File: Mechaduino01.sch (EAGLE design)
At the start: 70 parts, among them IC1 SAMD21G18A-AUT, IC2 AP2202-ADJ, Q1 2.5A/30V, Q2 NFET, Q3 BSS138, Q4 BSS138, Q5 BSS138, U3 74AHC1G125, Y1 32,768Khz

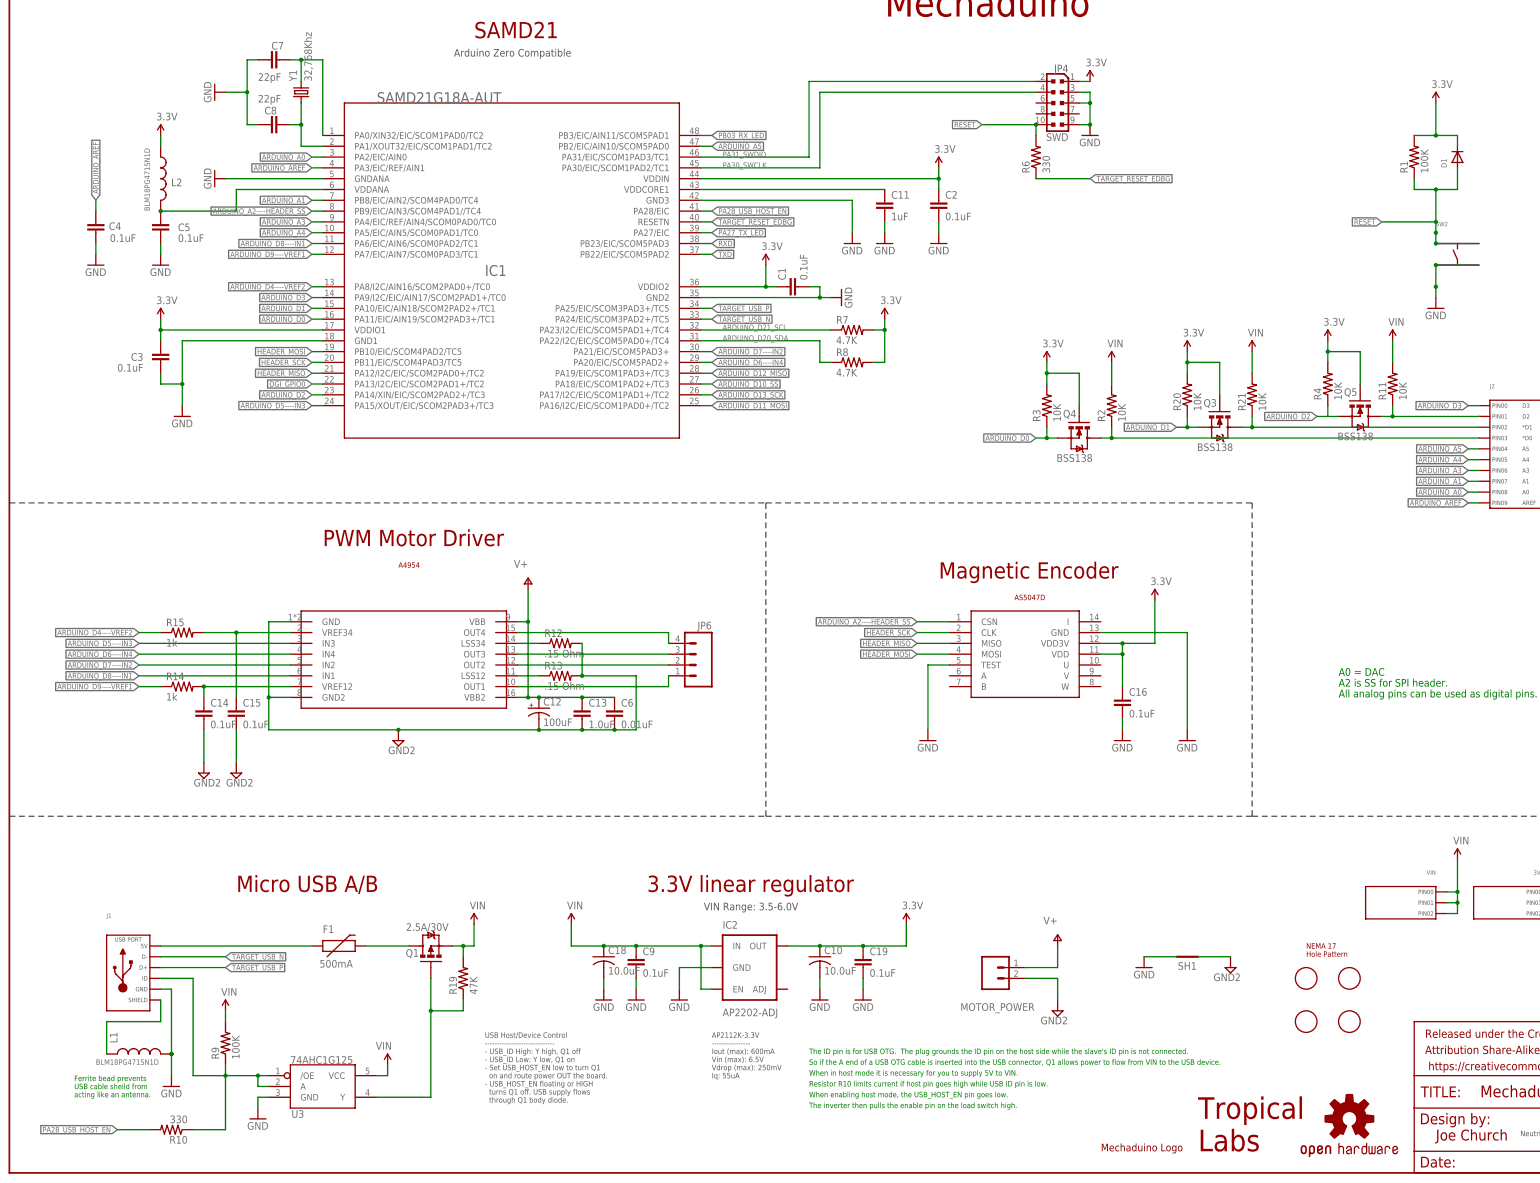
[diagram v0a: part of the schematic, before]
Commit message: moved IO headers down 0.01
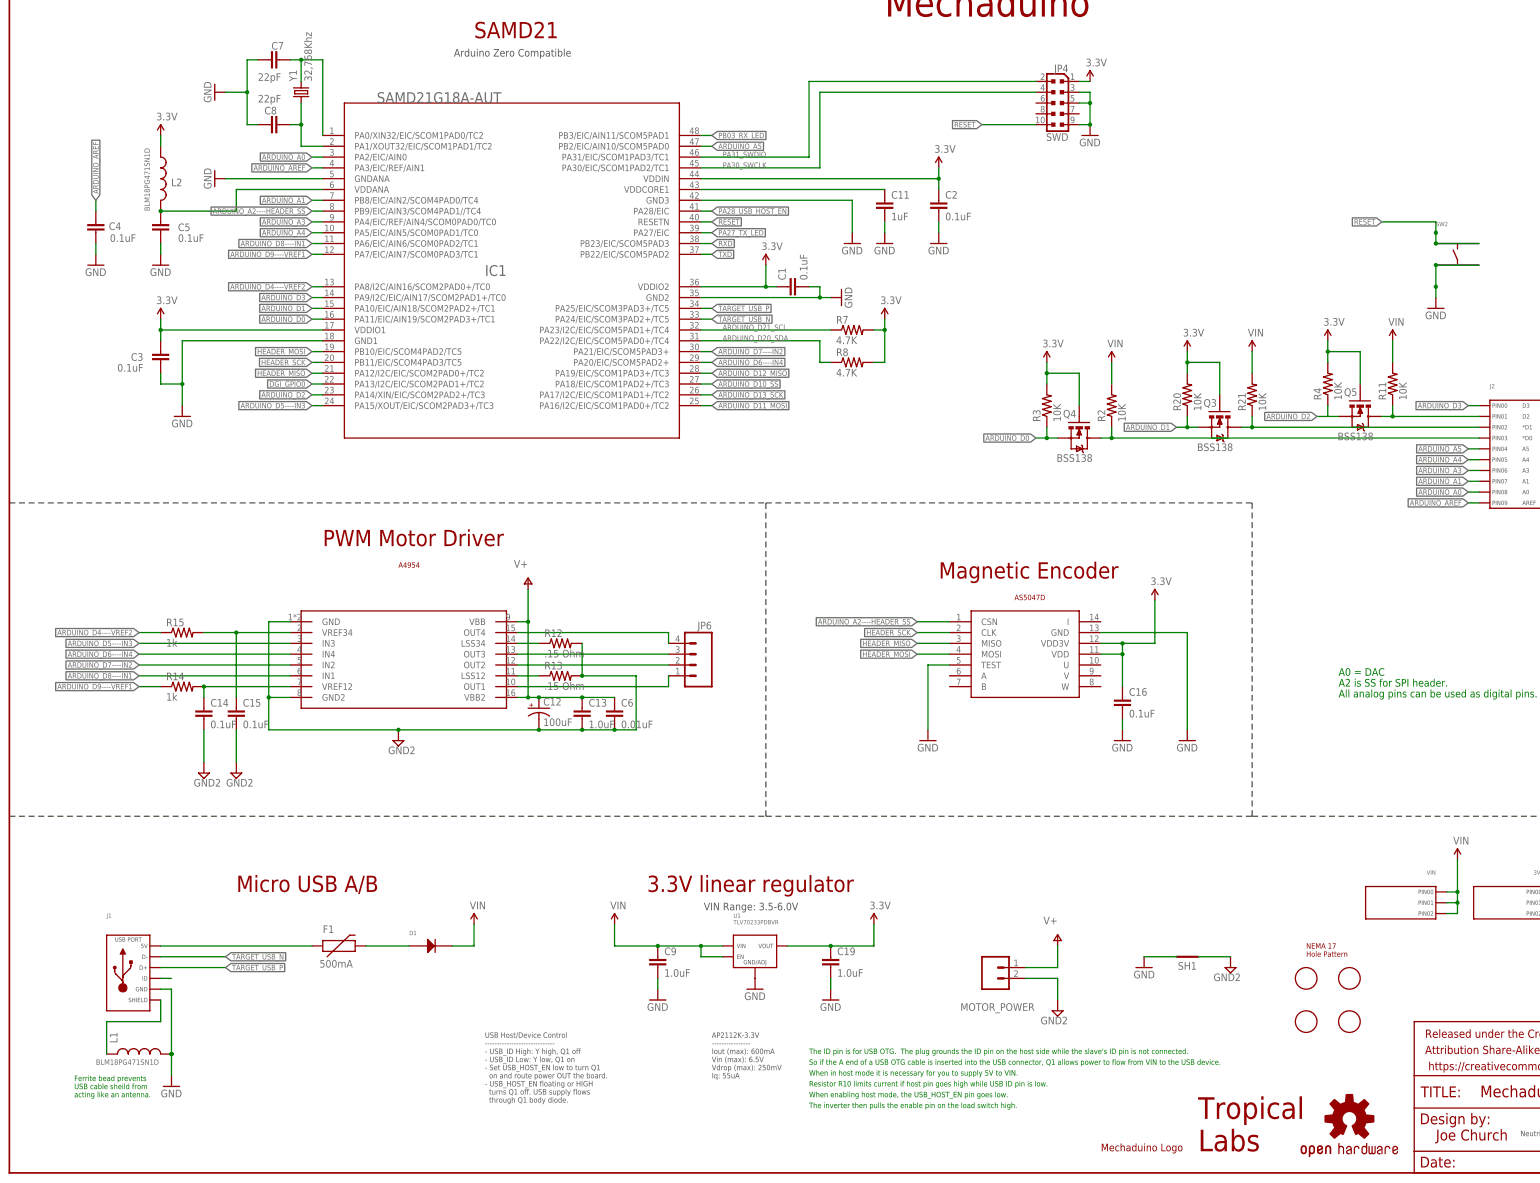
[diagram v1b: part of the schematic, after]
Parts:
- removed C10, C18: 10.0uF, rcl:C-USC0805
- removed IC2: AP2202-ADJ, SparkFun-PowerIC:AP2202-ADJ
- removed Q1: 2.5A/30V, SparkFun-DiscreteSemi:MOSFET-PCHANNELDMG2307L
- removed R1, R9: 100K, adafruit:R-US_R0402-VISHAY
- removed R10, R6: 330, adafruit:R-US_R0402-VISHAY
- removed R19: 47K, SparkFun-Resistors:47KOHM1/10W1%(0603)
- removed U3: 74AHC1G125, SparkFun-DigitalIC:74AHC1G125
- added U1: TLV70233PDBVR, MF_IC_Power:TLV70233PDBVR
- C19, C9: value 0.1uF -> 1.0uF
- D1: device adafruit:DIODESOD-523 -> MF_Discrete_Semiconductor:DIODE_SMA
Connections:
- removed net N$34: Q1.G, R19.1, U3.Y
- removed net TARGET_RESET_EDBG: IC1.RESETN, R6.1
- net 3.3V: now also U1.VOUT; no longer C10.1, D1.C, IC2.OUT, R1.2
- net GND: now also U1.GND/ADJ; no longer C10.2, C18.2, IC2.GND, U3.GND
- net N$33: now also D1.ANODE; no longer Q1.D
- net N$7: no longer R10.1, R9.1, U3./OE, U3.A
- net PA28_USB_HOST_EN: no longer R10.2
- net RESET: now also IC1.RESETN; no longer D1.A, R1.1, R6.2
- net VIN: now also D1.CATHODE, U1.EN, U1.VIN; no longer C18.1, IC2.EN, IC2.IN, Q1.S, R19.2, R9.2, U3.VCC
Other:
- moved on the sheet: C19, C9, D1

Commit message: moved things around
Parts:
- D1: device MF_Discrete_Semiconductor:DIODE_SMA -> MF_Discrete_Semiconductor:DIODE_SOD-123
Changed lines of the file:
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@@
 <part name="R11" library="adafruit" deviceset="R-US_" device="R0402-VISHAY" value="10K"/>
 <part name="U1" library="MF_IC_Power" deviceset="TLV702" device="33PDBVR"/>
-<part name="D1" library="MF_Discrete_Semiconductor" deviceset="DIODE" device="_SMA"/>
+<part name="D1" library="MF_Discrete_Semiconductor" deviceset="DIODE" device="_SOD-123"/>
 </parts>
 <sheets>

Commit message: commit after rollback issues
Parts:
- added Q1: BSS138, SparkFun:MOSFET-NCHANNELSMD
- added R1, R6: 10K, adafruit:R-US_R0402-VISHAY
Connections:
- new net HV4: J2.PIN0, Q1.D, R6.1
- net 3.3V: now also Q1.G, R1.2
- net ARDUINO_D3: now also Q1.S, R1.1; no longer J2.PIN0
- net VIN: now also R6.2
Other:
- moved on the sheet: Q3, Q4, Q5, R11, R2, R20, R21, R3, R4

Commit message: updated caps
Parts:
- C7, C8: value 22pF -> 18pF
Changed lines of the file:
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@@
 <part name="C5" library="swift" deviceset="CAP" device="0402" value="0.1uF"/>
 <part name="GND41" library="PowerTags" deviceset="GND" device=""/>
-<part name="C7" library="swift" deviceset="CAP" device="0402" value="22pF"/>
-<part name="C8" library="swift" deviceset="CAP" device="0402" value="22pF"/>
+<part name="C7" library="swift" deviceset="CAP" device="0402" value="18pF"/>
+<part name="C8" library="swift" deviceset="CAP" device="0402" value="18pF"/>
 <part name="LED1" library="Opto" deviceset="0044_KPT-2012YC" device="" value="Green"/>
 <part name="R7" library="adafruit" deviceset="R-US_" device="R0402-VISHAY" value="4.7K"/>

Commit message: reday to order
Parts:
- LOGO4: value OSHW-LOGOL-COPPER -> OSHW-LOGOMOD; device SparkFun-Aesthetics:OSHW-LOGOL-COPPER -> SparkFun-Aesthetics:OSHW-LOGOMOD
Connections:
- new net A: U$4.A
- new net B: U$4.B
- new net I: U$4.I
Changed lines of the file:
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@@
 <grid distance="0.1" unitdist="inch" unit="inch" style="lines" multiple="1" display="no" altdistance="0.01" altunitdist="inch" altunit="inch"/>
 <layers>
-<layer number="1" name="Top" color="4" fill="1" visible="no" active="no"/>
-<layer number="16" name="Bottom" color="1" fill="1" visible="no" active="no"/>
-<layer number="17" name="Pads" color="2" fill="1" visible="no" active="no"/>
-<layer number="18" name="Vias" color="2" fill="1" visible="no" active="no"/>
-<layer number="19" name="Unrouted" color="15" fill="1" visible="no" active="no"/>
-<layer number="20" name="Dimension" color="15" fill="1" visible="no" active="no"/>
-<layer number="21" name="tPlace" color="7" fill="1" visible="no" active="no"/>
-<layer number="22" name="bPlace" color="15" fill="1" visible="no" active="no"/>
-<layer number="23" name="tOrigins" color="15" fill="1" visible="no" active="no"/>
-<layer number="24" name="bOrigins" color="15" fill="1" visible="no" active="no"/>
-<layer number="25" name="tNames" color="10" fill="1" visible="no" active="no"/>
-<layer number="26" name="bNames" color="7" fill="1" visible="no" active="no"/>
-<layer number="27" name="tValues" color="7" fill="1" visible="no" active="no"/>
-<layer number="28" name="bValues" color="7" fill="1" visible="no" active="no"/>
+<layer number="1" name="Top" color="4" fill="1" visible="yes" active="no"/>
+<layer number="16" name="Bottom" color="1" fill="1" visible="yes" active="no"/>
+<layer number="17" name="Pads" color="2" fill="1" visible="yes" active="no"/>
+<layer number="18" name="Vias" color="2" fill="1" visible="yes" active="no"/>
+<layer number="19" name="Unrouted" color="15" fill="1" visible="yes" active="no"/>
+<layer number="20" name="Dimension" color="15" fill="1" visible="yes" active="no"/>
+<layer number="21" name="tPlace" color="7" fill="1" visible="yes" active="no"/>
+<layer number="22" name="bPlace" color="15" fill="1" visible="yes" active="no"/>
+<layer number="23" name="tOrigins" color="15" fill="1" visible="yes" active="no"/>
+<layer number="24" name="bOrigins" color="15" fill="1" visible="yes" active="no"/>
+<layer number="25" name="tNames" color="10" fill="1" visible="yes" active="no"/>
+<layer number="26" name="bNames" color="7" fill="1" visible="yes" active="no"/>
+<layer number="27" name="tValues" color="7" fill="1" visible="yes" active="no"/>
+<layer number="28" name="bValues" color="7" fill="1" visible="yes" active="no"/>
 <layer number="29" name="tStop" color="7" fill="3" visible="no" active="no"/>
 <layer number="30" name="bStop" color="7" fill="6" visible="no" active="no"/>
@@
 <layer number="35" name="tGlue" color="7" fill="4" visible="no" active="no"/>
 <layer number="36" name="bGlue" color="7" fill="5" visible="no" active="no"/>
-<layer number="37" name="tTest" color="7" fill="1" visible="no" active="no"/>
-<layer number="38" name="bTest" color="7" fill="1" visible="no" active="no"/>
+<layer number="37" name="tTest" color="7" fill="1" visible="yes" active="no"/>
+<layer number="38" name="bTest" color="7" fill="1" visible="yes" active="no"/>
 <layer number="39" name="tKeepout" color="4" fill="11" visible="no" active="no"/>
 <layer number="40" name="bKeepout" color="1" fill="11" visible="no" active="no"/>
@@
 <layer number="44" name="Drills" color="7" fill="1" visible="no" active="no"/>
 <layer number="45" name="Holes" color="7" fill="1" visible="no" active="no"/>
-<layer number="46" name="Milling" color="3" fill="1" visible="no" active="no"/>
-<layer number="47" name="Measures" color="7" fill="1" visible="no" active="no"/>
-<layer number="48" name="Document" color="7" fill="1" visible="no" active="no"/>
-<layer number="49" name="Reference" color="7" fill="1" visible="no" active="no"/>
-<layer number="50" name="dxf" color="12" fill="1" visible="no" active="no"/>
-<layer number="51" name="tDocu" color="7" fill="1" visible="no" active="no"/>
-<layer number="52" name="bDocu" color="7" fill="1" visible="no" active="no"/>
-<layer number="53" name="tGND_GNDA" color="7" fill="1" visible="no" active="no"/>
-<layer number="54" name="bGND_GNDA" color="7" fill="1" visible="no" active="no"/>
-<layer number="56" name="wert" color="7" fill="1" visible="no" active="no"/>
-<layer number="57" name="tCAD" color="7" fill="1" visible="no" active="no"/>
-<layer number="59" name="tCarbon" color="7" fill="1" visible="no" active="no"/>
-<layer number="60" name="bCarbon" color="7" fill="1" visible="no" active="no"/>
+<layer number="46" name="Milling" color="3" fill="1" visible="yes" active="no"/>
+<layer number="47" name="Measures" color="7" fill="1" visible="yes" active="no"/>
+<layer number="48" name="Document" color="7" fill="1" visible="yes" active="no"/>
+<layer number="49" name="Reference" color="7" fill="1" visible="yes" active="no"/>
+<layer number="50" name="dxf" color="12" fill="1" visible="yes" active="no"/>
+<layer number="51" name="tDocu" color="7" fill="1" visible="yes" active="no"/>
+<layer number="52" name="bDocu" color="7" fill="1" visible="yes" active="no"/>
+<layer number="53" name="tGND_GNDA" color="7" fill="1" visible="yes" active="no"/>
+<layer number="54" name="bGND_GNDA" color="7" fill="1" visible="yes" active="no"/>
+<layer number="56" name="wert" color="7" fill="1" visible="yes" active="no"/>
+<layer number="57" name="tCAD" color="7" fill="1" visible="yes" active="no"/>
+<layer number="59" name="tCarbon" color="7" fill="1" visible="yes" active="no"/>
+<layer number="60" name="bCarbon" color="7" fill="1" visible="yes" active="no"/>
 <layer number="90" name="Modules" color="5" fill="1" visible="yes" active="yes"/>
 <layer number="91" name="Nets" color="2" fill="1" visible="yes" active="yes"/>
@@
 <part name="SUPPLY21" library="SparkFun-Aesthetics" deviceset="3.3V" device=""/>
 <part name="GND4" library="supply1" deviceset="GND" device=""/>
-<part name="LOGO4" library="SparkFun-Aesthetics" deviceset="OSHW-LOGO" device="L-COPPER" value="OSHW-LOGOL-COPPER"/>
+<part name="LOGO4" library="SparkFun-Aesthetics" deviceset="OSHW-LOGO" device="MOD" value="OSHW-LOGOMOD"/>
 <part name="SUPPLY6" library="SparkFun-Aesthetics" deviceset="VIN" device=""/>
 <part name="SUPPLY22" library="SparkFun-Aesthetics" deviceset="3.3V" device=""/>
@@
 <instance part="R15" gate="G$1" x="43.18" y="129.54"/>
 <instance part="JP6" gate="G$1" x="162.56" y="121.92" rot="MR0"/>
-<instance part="GND22" gate="1" x="218.44" y="104.14"/>
+<instance part="GND22" gate="1" x="210.82" y="104.14"/>
 <instance part="C16" gate="G$1" x="264.16" y="111.76"/>
 <instance part="GND23" gate="1" x="264.16" y="104.14"/>
@@
 <segment>
 <pinref part="U$4" gate="G$1" pin="TEST"/>
-<wire x1="223.52" y1="121.92" x2="218.44" y2="121.92" width="0.1524" layer="91"/>
+<wire x1="223.52" y1="121.92" x2="210.82" y2="121.92" width="0.1524" layer="91"/>
 <pinref part="GND22" gate="1" pin="GND"/>
-<wire x1="218.44" y1="106.68" x2="218.44" y2="121.92" width="0.1524" layer="91"/>
+<wire x1="210.82" y1="106.68" x2="210.82" y2="121.92" width="0.1524" layer="91"/>
 </segment>
 <segment>
@@
 </segment>
 </net>
+<net name="I" class="0">
+<segment>
+<pinref part="U$4" gate="G$1" pin="I"/>
+<wire x1="259.08" y1="132.08" x2="261.62" y2="132.08" width="0.1524" layer="91"/>
+</segment>
+</net>
+<net name="A" class="0">
+<segment>
+<pinref part="U$4" gate="G$1" pin="A"/>
+<wire x1="223.52" y1="119.38" x2="220.98" y2="119.38" width="0.1524" layer="91"/>
+<label x="215.9" y="119.38" size="1.778" layer="95"/>
+</segment>
+</net>
+<net name="B" class="0">
+<segment>
+<pinref part="U$4" gate="G$1" pin="B"/>
+<wire x1="223.52" y1="116.84" x2="220.98" y2="116.84" width="0.1524" layer="91"/>
+<label x="215.9" y="116.84" size="1.778" layer="95"/>
+</segment>
+</net>
